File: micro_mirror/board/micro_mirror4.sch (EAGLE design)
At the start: 143 parts, among them IC1 74LV7014, IC2 74LV02, IC3 74LV08, IC5 LM324D, J1 POWER_JACKPTH_LOCK, U8 TPS62160, X1 SMA-142-0701-801/806, X2 SMA-142-0701-801/806, X3 SMA-142-0701-801/806, X4 SMA-142-0701-801/806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

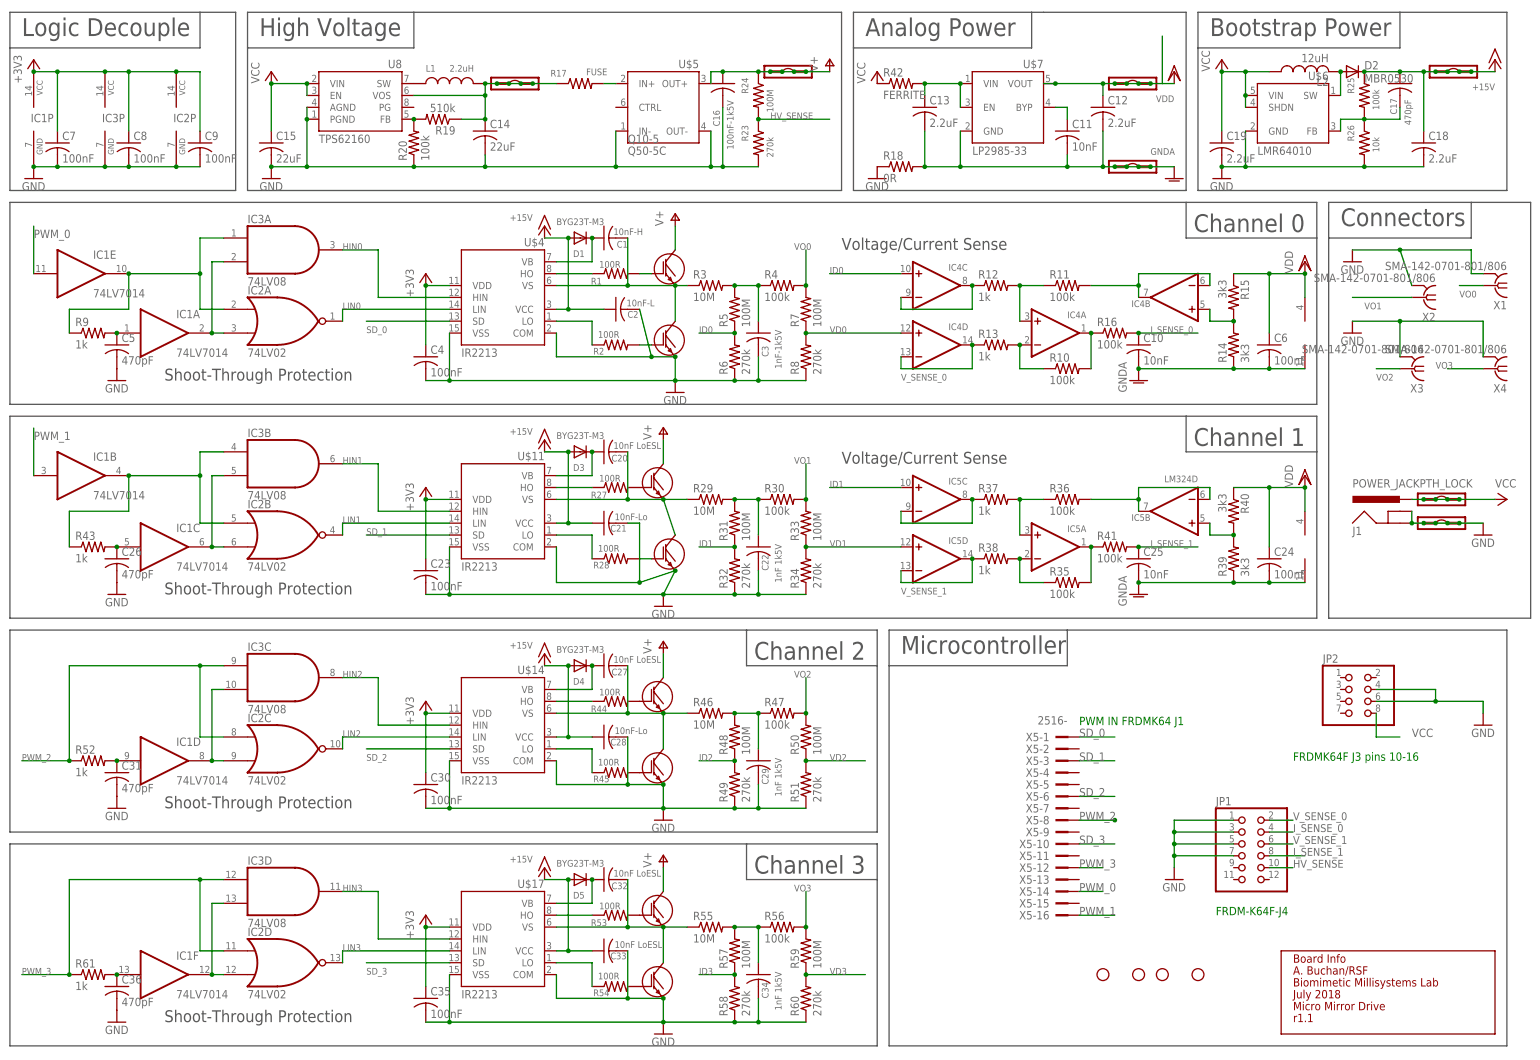
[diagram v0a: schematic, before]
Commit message: cleaning up schematic warnings
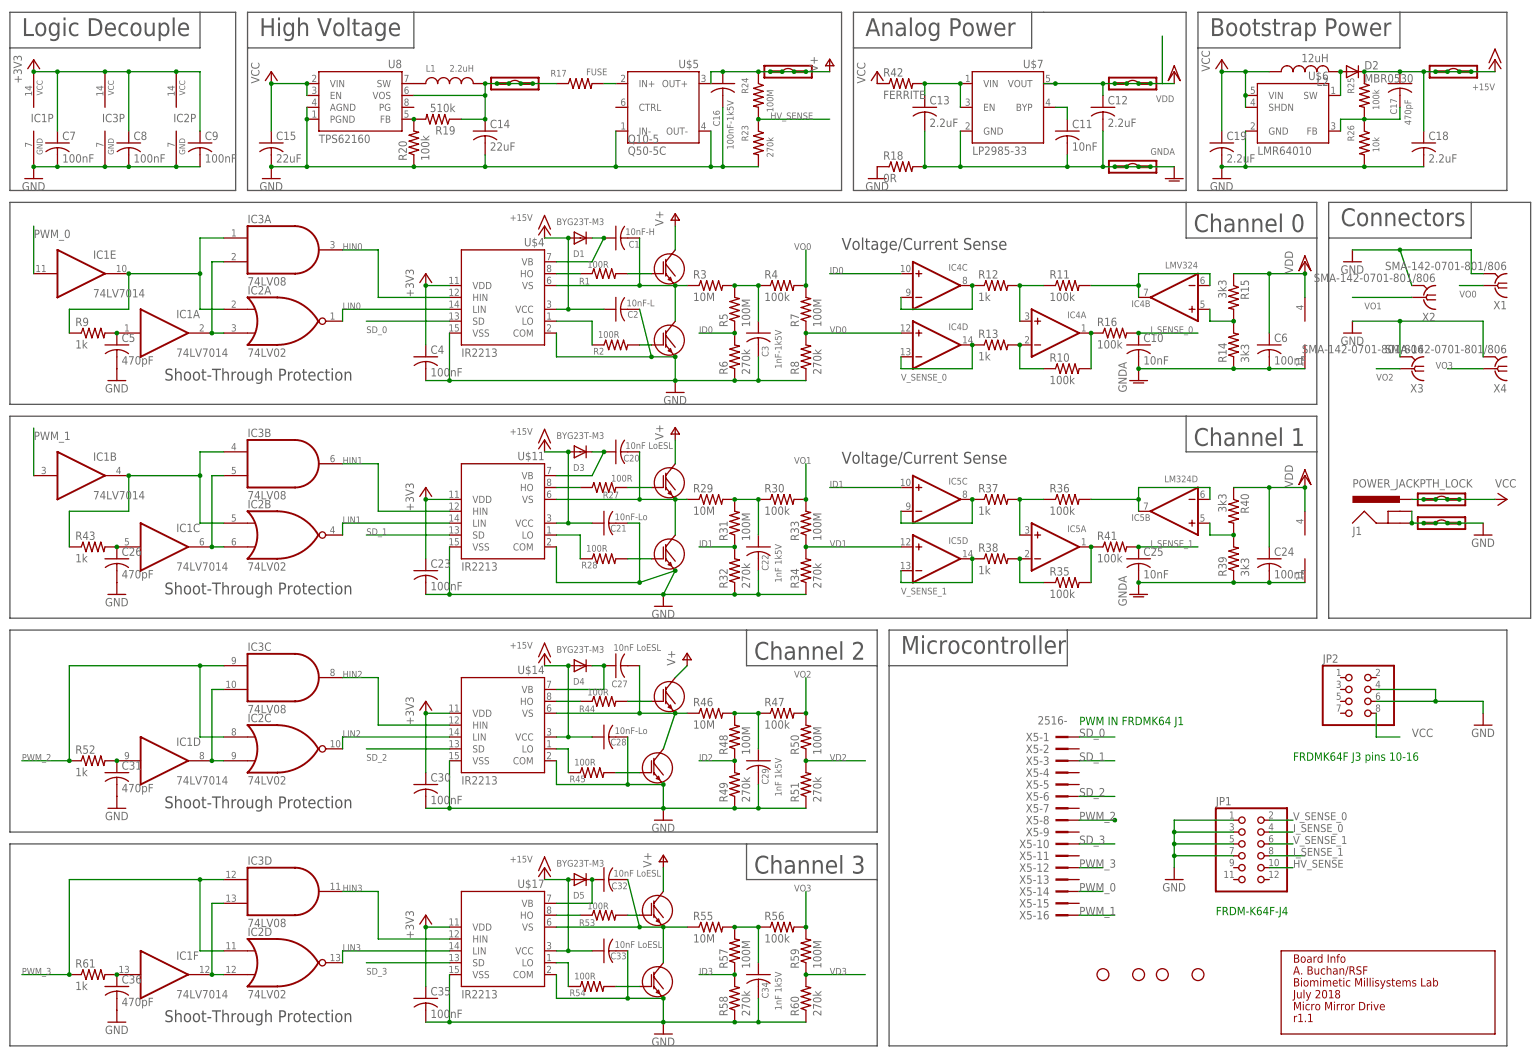
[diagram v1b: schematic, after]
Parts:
- IC4: value (none) -> LMV324
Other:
- moved on the sheet: C1, C20, C27, R1, R27, R28, R44, R45, R53, R54

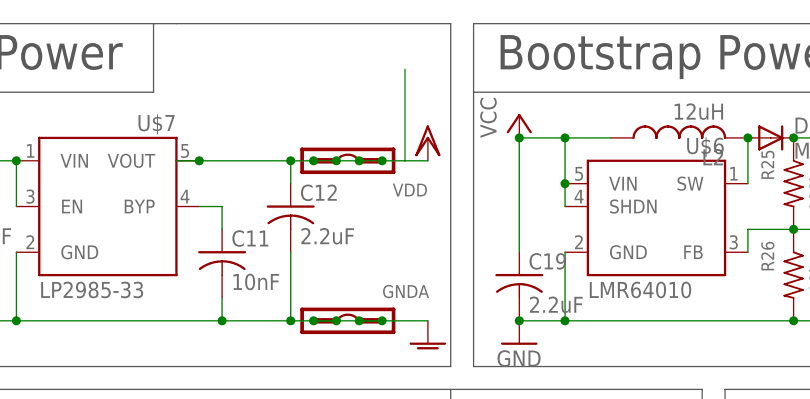
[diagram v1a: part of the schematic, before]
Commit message: still need to do correct merge of vdd and vdda
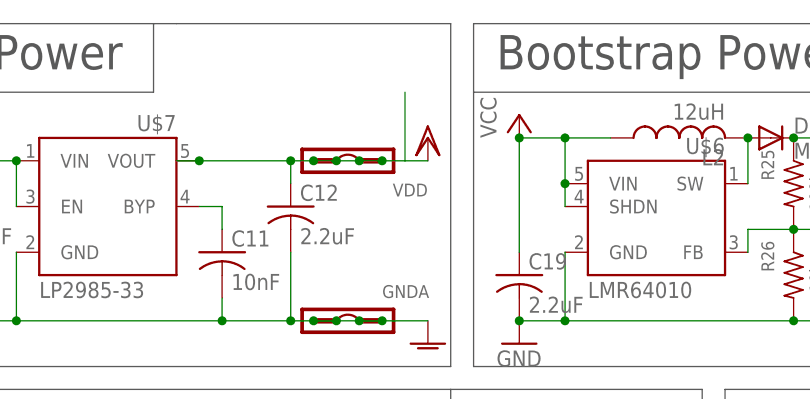
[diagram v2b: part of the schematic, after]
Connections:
- net +3V3 renamed VDDA
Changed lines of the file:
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@@
 </segment>
 </net>
-<net name="+3V3" class="0">
+<net name="VDDA" class="0">
 <segment>
 <pinref part="C7" gate="G$1" pin="1"/>
@@
 <wire x1="248.92" y1="154.94" x2="259.08" y2="154.94" width="0.1524" layer="91"/>
 <junction x="248.92" y="154.94"/>
-<wire x1="271.78" y1="154.94" x2="271.78" y2="165.1" width="0.1524" layer="91"/>
+<wire x1="271.78" y1="154.94" x2="271.78" y2="162.56" width="0.1524" layer="91"/>
 </segment>
 </net>

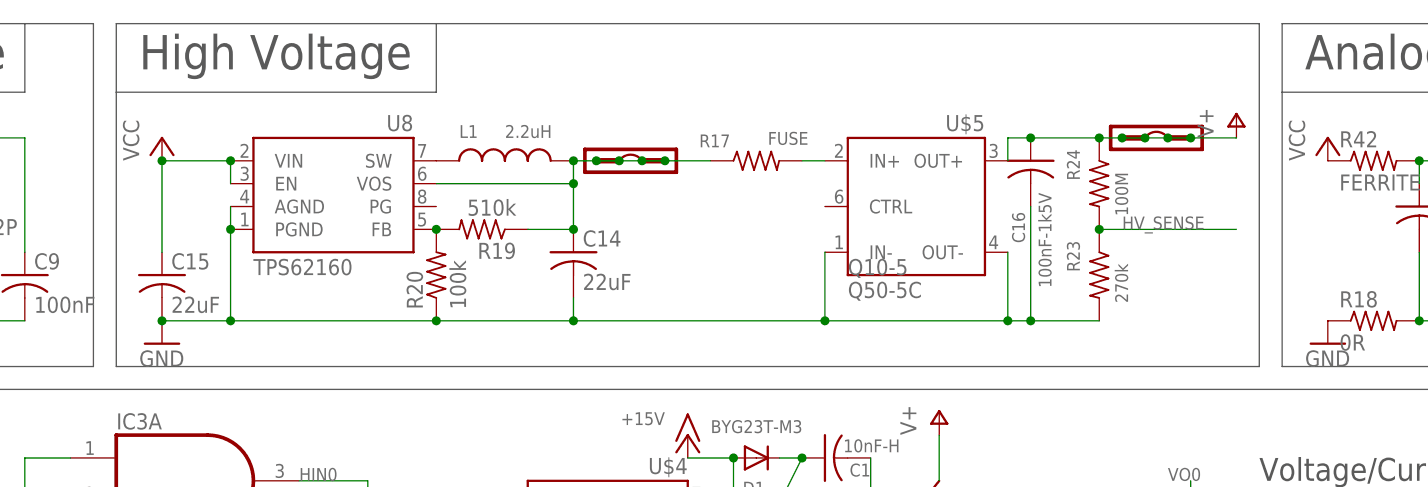
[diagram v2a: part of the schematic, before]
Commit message: added voltage divider for HV out in case needed
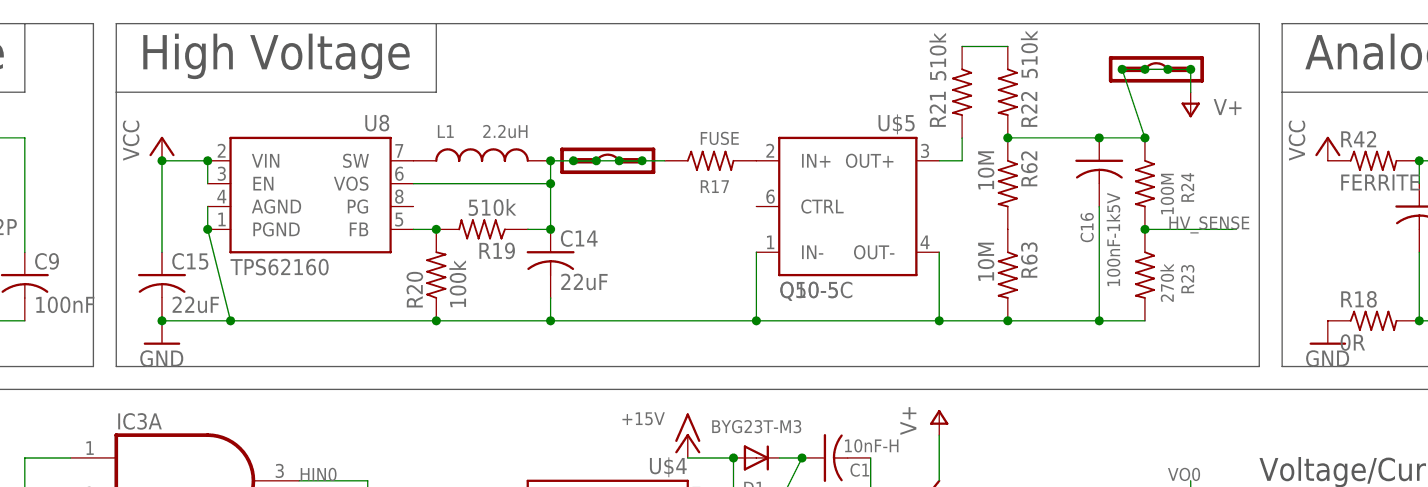
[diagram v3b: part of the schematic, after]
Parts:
- added R21, R22: 510k, rcl:R-US_R1206
- added R62, R63: 10M, rcl:R-US_R1206
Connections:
- new net N$24: R21.1, R22.1
- new net N$60: R21.2, U$5.OUT+
- new net N$62: R62.2, R63.1
- net GND: now also R63.2
- net V+: now also R22.2, R62.1; no longer U$5.OUT+
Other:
- moved on the sheet: C14, C16, L1, R17, R23, R24, U$5, U8
